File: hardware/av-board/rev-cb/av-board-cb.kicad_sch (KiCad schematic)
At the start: 291 parts, among them J1 RCA Y, J11 XIAO 5V..D7, J12 XIAO D0..D6, J13 OPTICAL, J14 RCA S/PDIF, J15 USB-C 5V, J16 JTAG, J2 RCA Pb, J20 DF40HC(3.0)-80DS, J21 DF40HC(3.0)-100DS, J22 DF40HC(3.0)-100DS, J3 RCA Pr, J4 RCA L, J5 RCA R, J6 HDMI-001, J7 SYNC, J8 VGA, Q1 2N7002, Q2 2N7002, Q3 2N7002, Q4 2N7002, Q5 2N7002, SW1 TS-1187A-B-A-B, SW2 TS-1187A-B-A-B, SW3 TS-1187A-B-A-B, U1 ADV7181DBCPZ-RL, U10 TPD4E05U06DQAR, U12 TPS7A2045PDBVR, U13 SN74LVC1GU04DBVR, U14 SN74LVC1G04DBVR, U15 SN74LVC1G04DBVR, U17 MS5351M, U18 ME6211C25M5G-N, U19 TPD4E05U06DQAR, U2 SN65DP159RGZR, U20 TPD4E05U06DQAR, U21 SN74LVC2G17DBVR, U22 SN74LVC8T245PWR, U23 SN74AVC4T245PWR, U24 ME6211C30M5G-N, U3 PCM1808PWR, U4 TLV62569DBVR, U5 TPS7A7001DDAR, U6 TPS7A7001DDAR, U7 TLV62569DBVR, U8 TPD4E05U06DQAR, U9 TPD4E05U06DQAR, Y1 28.63636MHz 20pF, Y2 25MHz 10pF

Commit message: AV boards: the last complete, valid design of each revision; decoupling at the pins
Each revision's board, schematic, fab files and renders are its last complete
route: DRC clean, no unconnected items, ERC clean, the board equal to its
schematic part for part (pads, values, footprints; only the mounting holes
H1-H4 have no symbol).

- Rev A: the silkscreen pass (labels clear of pads, texts and part bodies);
  copper unchanged.
- Rev B: the previous route with the silkscreen pass. Its schematic stays the
  one it was routed from: board.py now numbers eight capacitors the other way
  round, and its placement fixes (below) are not routed yet, the routes on the
  new placement having left 1 and 3 connections (review.md, Status).
- C-A: routed again on the fixed placement (try-ca-p1), the copper the router
  laid twice over taken up (218 segments).
- C-B: S/PDIF on rev B's 5-pin header instead of the coax jack, the HDMI
  receptacle next to the RCAs, the board 100 x 100 mm; routed again on the
  fixed placement (try-cb-p3). 5.4 mm of copper laid side by side in five
  nets is left (rev-c/review.md).

The review found decoupling not at the pins on every board (ADV7511 9-25 mm,
DP159 6-13 mm, the bucks' input capacitor by EN, the LDOs' capacitors, the
clock LDOs 73-80 mm from their chip) and C's VBUS_IN 0.25 mm wide for 2 A:
- parts.py: Part.at = "REF.PAD", the one pad a capacitor or filter serves;
  circuits, carrier.py and board.py name it for every regulator and supply pin
- pcbkit.py placer: ESD parts first, then small chips, then the at= capacitors
  and bias parts in board.py order; mean pin-to-capacitor distance on the
  placements: rev B 8.1 -> 3.6 mm, C-A 6.3 -> 3.3, C-B 5.5 -> 3.4
- rev C: VBUS_IN 0.7/1.2 mm into the TVS and fuse; rev B and C: the coax
  slicer placed first (SPDIF_AC a bias net); rev B: the buck U4 turned over

Kit: the silkscreen pass (labels clear of pads, texts, parts and the SOM,
reserved in the placer); prune takes up copper lying on another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
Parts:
- removed J14: RCA S/PDIF, lcsc:CONN-TH_RCJ-011, symbol lcsc:RCJ-017
- C11, C8: value 10u -> 220p; footprint Capacitor_SMD:C_0805_2012Metric -> Capacitor_SMD:C_0402_1005Metric; LCSC C15850 -> C1530
- C12, C9: value 220p -> 10u; footprint Capacitor_SMD:C_0402_1005Metric -> Capacitor_SMD:C_0805_2012Metric; LCSC C1530 -> C15850
- C5, C85: value 10u -> 6.8p; footprint Capacitor_SMD:C_0805_2012Metric -> Capacitor_SMD:C_0402_1005Metric; LCSC C15850 -> C1576
- C6, C86: value 6.8p -> 10u; footprint Capacitor_SMD:C_0402_1005Metric -> Capacitor_SMD:C_0805_2012Metric; LCSC C1576 -> C15850
- J13: value OPTICAL -> SPDIF; footprint lcsc:HDR-TH_3P-P2.54-V-M_PZ254V-11-03P -> lcsc:HDR-TH_5P-P2.54-V-M; symbol lcsc:PZ254V-11-03P_C2937625 -> lcsc:PZ254V-11-05P; LCSC C2937625 -> C492404
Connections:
- net FB_1V1: now also C85.2; no longer C86.2
- net FB_1V8A: now also C11.2; no longer C12.2
- net FB_3V3: now also C8.2; no longer C9.2
- net FB_3V6: now also C5.2; no longer C6.2
- net GND: now also C12.2, C6.2, C86.2, C9.2, J13.4; no longer C11.2, C5.2, C8.2, C85.2
- net IN_KEY1: now also J20.75; no longer J21.5
- net IN_KEY2: now also J20.73; no longer J21.7
- net IN_LED: now also J20.71; no longer J21.11
- net SPDIF_5V: now also J13.5; no longer J13.3
- net SPDIF_COAX: now also J13.1
- net SPDIF_OPT: now also J13.3; no longer J13.1
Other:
- moved on the sheet: C11, C12, C5, C6, C65, C66, C67, C68, C69, C8, C80, C81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

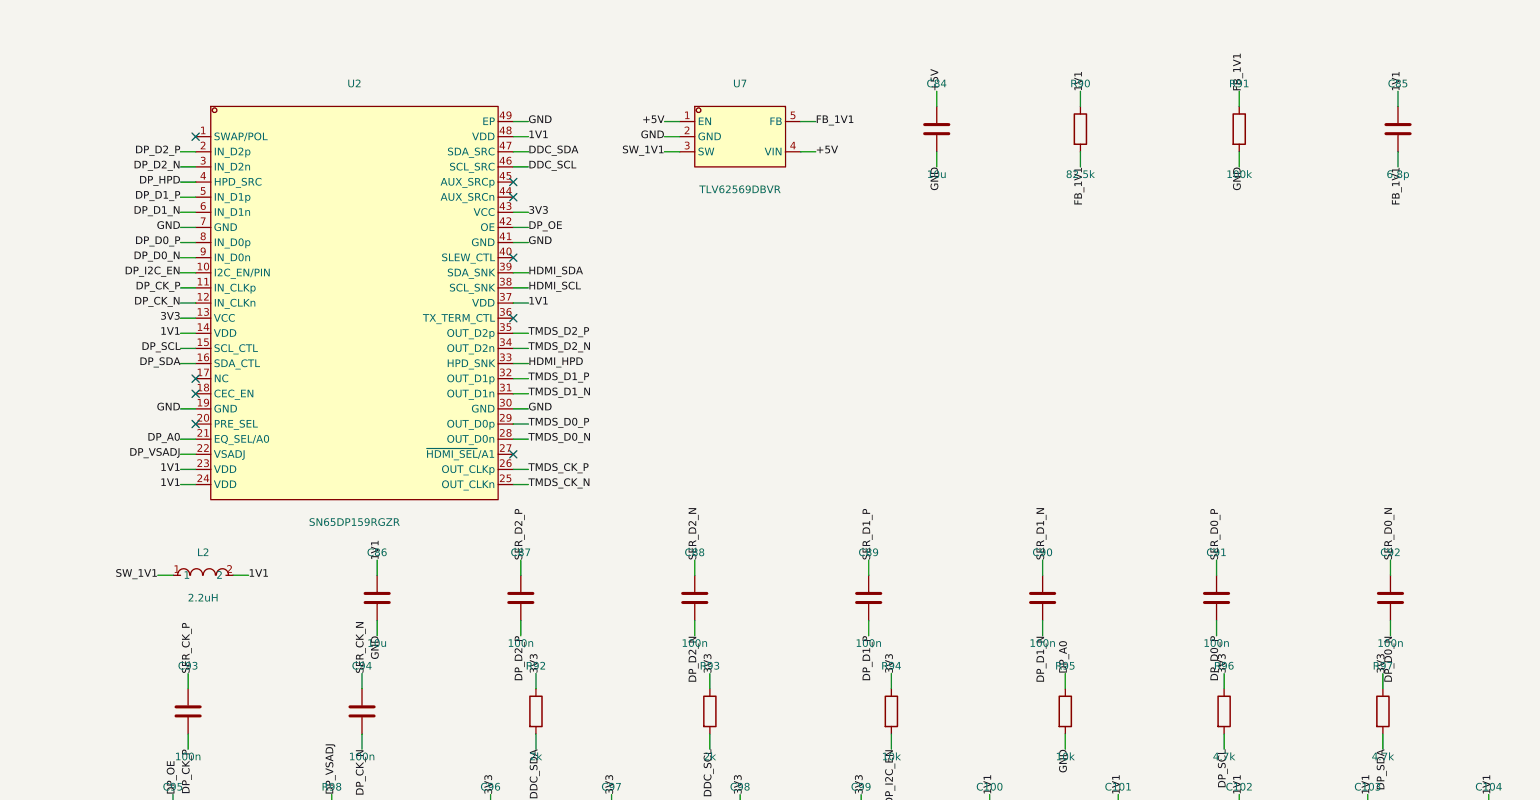
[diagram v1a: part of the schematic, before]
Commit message: AV boards: rev B, C-B routed on the fixed placement; prune side-by-side copies; JLC jack rotation
Every revision: schematic = board.py, the board = its schematic part for part,
ERC and DRC clean, no unconnected items; rev B's, C-A's and C-B's review tables
measured on these routes.

- Rev B: routed on the capacitor placement fixes (try-b-r1, its last gap
  finished); schematic regenerated (eight capacitors renumbered).
- C-B: the 1V1 buck's inductor and output capacitor placed before its feedback
  divider: in the 3V6 bucks' order the divider's 6.8 pF took the inductor's place
  beside SW, the inductor went above the chip with its SW pad turned away (10.7 mm
  of SW track, FB's copper 0.2 mm from it). Routed again (try-cb-q3): SW 4.1 mm,
  FB 3.0 mm from it; nothing digital within 0.5 mm of an analog line but XTAL1
  beside LLC at the pins' pitch.
- C-A: its review column measured on the route; CPL jack rotations.
- kit/pcbkit.py prune: copper laid side by side taken up too (beside(): the
  shorter of each kit/doubled.py pair), every candidate checked by DRC on a copy
  of the file's text first (save_without(), removable()), so nothing taken out of
  a pcbnew board is put back; rounds run with faulthandler and report a crash's
  signal (one round had segfaulted in libstdc++ with no message).
- kit/pcbkit.py finish_unconnected: a gap's three nearest pad pairs tried in turn
  (rev B's TX_PLVDD pin 21 was walled in towards pin 26, not towards its own
  capacitor).
- kit/gen_fab.py JLC_TURN: JLCPCB places a part by its own footprint for the LCSC
  number; for RCJ-014 and RCJ-017 that is ours turned 90 degrees, so the CPL
  turns those jacks back (their preview had the barrels along the board edge).
  RCJ-012 has no footprint there and is placed as drawn.

Co-Authored-By: Claude Opus 5.5 <noreply@anthropic.com>
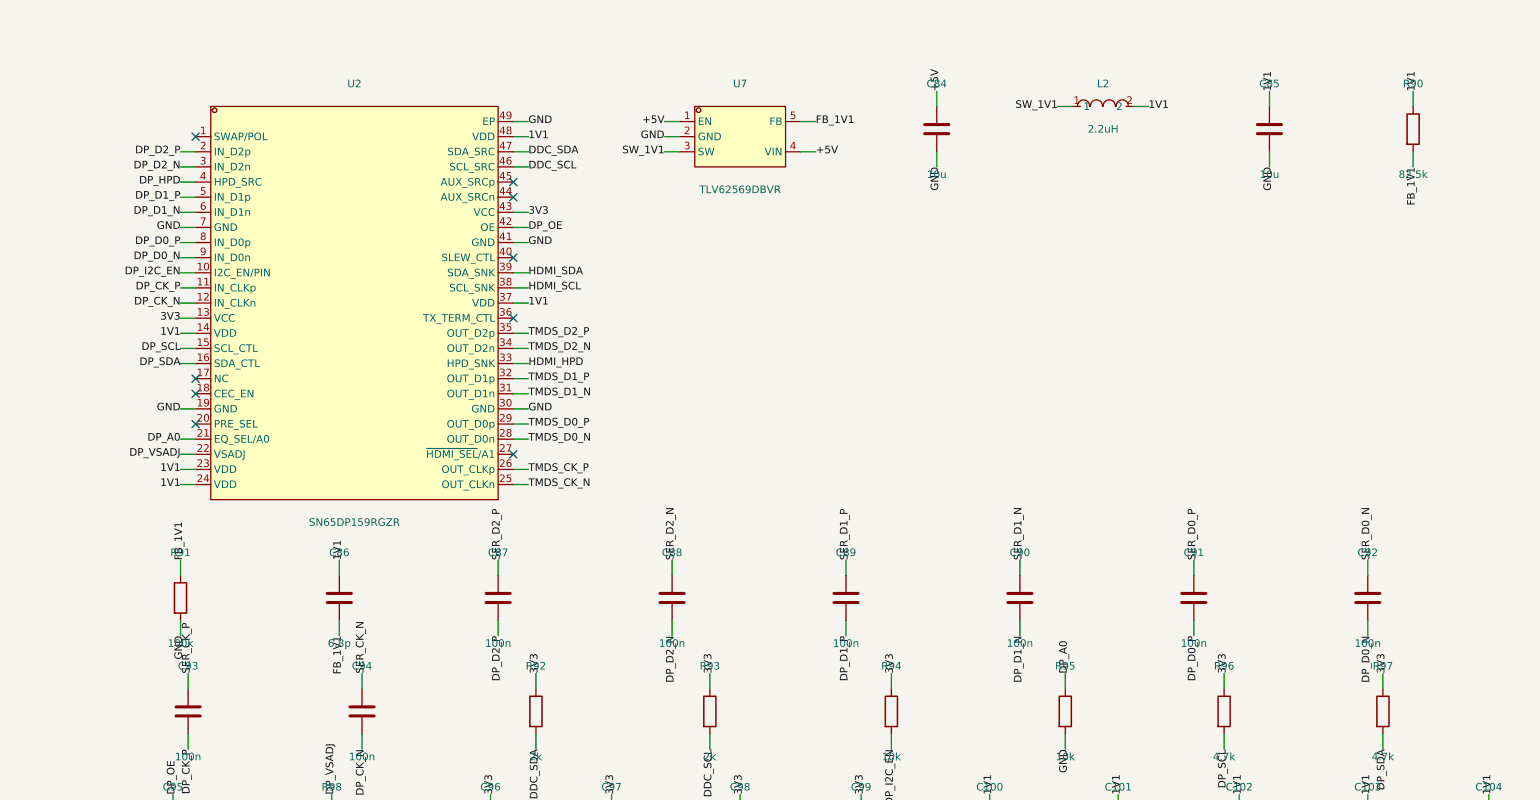
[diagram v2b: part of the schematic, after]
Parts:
- C85: value 6.8p -> 10u; footprint Capacitor_SMD:C_0402_1005Metric -> Capacitor_SMD:C_0805_2012Metric; LCSC C1576 -> C15850
- C86: value 10u -> 6.8p; footprint Capacitor_SMD:C_0805_2012Metric -> Capacitor_SMD:C_0402_1005Metric; LCSC C15850 -> C1576
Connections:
- net FB_1V1: now also C86.2; no longer C85.2
- net GND: now also C85.2; no longer C86.2
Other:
- moved on the sheet: C85, C86, C87, C88, C89, C90, C91, C92, L2, R90, R91

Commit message: AV board C-B: a protected debug header and test pads; the kit on KiCad 10, a second host
C-B (the SOM hides the FPGA's pins, so the board brings out what bring-up needs):
- J17, a 2 x 8 header left of the SOM: the ADV7181D's, the DP159's and the MS5351M's I2C, six
  spare FPGA pins, J22's nearest (dbg0-dbg5: AB16 L13 M13 AA16 AB17 Y17, LVCMOS33 in
  fpga/av-board-cb.cst), a 3.3 V reference and ground, labelled pin by pin, "DEBUG" above it.
  Every pin but ground through 220 R by the header (C25091, as Digilent's Pmod ports): a slipped
  probe or a wrong wire drives at most 15 mA into a pin; VREF, beside ground, is a reference
  (50 mW in its resistor when shorted), not a supply.
- A bare test pad on each rail by its regulator (+5V 3V6 3V3 1V8 1V1 3V0 2V5 5VA), labelled,
  and two ground pads with holes for a wire loop. Not assembled.
- The DP159's ground pins 19 and 41 now reach into its exposed pad: their fanout stubs stopped
  0.22 mm short of it, the prune pass took them up, and pin 19 was left open
  (gen_pcb.py serdes()).
- Re-routed: the best of a batch (v5): DRC 0 errors, 0 unconnected; schematic = board.py =
  board (1064 pins); fab files, renders and rev-c/review.md's layout numbers updated. Three
  resistors after the debug block are renumbered (R100-R102 -> R113-R115).
- Known, fixes next: an HDMI 2.0 layout audit against TI's SN65DP159 and SPRAAR7 guidelines
  finds other nets' vias against the TMDS run (their plane antipads within 0.01-0.21 mm),
  pairs 3W apart (TI: 5W), the transceivers' reference clock autorouted as two single lines,
  a crystal and a mounting hole near the lines, and no plane voids under the pads on them.

rev-c/review.md: kit/xtalk.py measures analog tracks against digital tracks only; KiCad's DRC
with the 0.5 mm rule as a custom rule counts vias too, and finds two of RCA_SYNC's vias 0.27 mm
from the VGA DDC clock on C-A (the C-A text said nothing but XTAL1/LLC came that close).

Kit:
- main(): the board made with its project (pcbn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
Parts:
- added J17: DEBUG, lcsc:HDR-TH_16P-P2.54-V-M-R2-C8-S2.54, symbol lcsc:Header-Male-2.54_2x8
- added R103, R104, R105, R106, R107, R108, R109, R110, R111, R112: 220, Resistor_SMD:R_0402_1005Metric, symbol Device:R
- added R113: 1k, Resistor_SMD:R_0402_1005Metric, symbol Device:R
- added R114, R115: 5.1k, Resistor_SMD:R_0402_1005Metric, symbol Device:R
- added TP1: +5V, TestPoint:TestPoint_Pad_D1.5mm, symbol Connector:TestPoint
- added TP10, TP9: GND, TestPoint:TestPoint_THTPad_D2.0mm_Drill1.0mm, symbol Connector:TestPoint
- added TP2: 3V6, TestPoint:TestPoint_Pad_D1.5mm, symbol Connector:TestPoint
- added TP3: 3V3, TestPoint:TestPoint_Pad_D1.5mm, symbol Connector:TestPoint
- added TP4: 1V8A, TestPoint:TestPoint_Pad_D1.5mm, symbol Connector:TestPoint
- added TP5: 1V1, TestPoint:TestPoint_Pad_D1.5mm, symbol Connector:TestPoint
- added TP6: 3V0, TestPoint:TestPoint_Pad_D1.5mm, symbol Connector:TestPoint
- added TP7: 2V5, TestPoint:TestPoint_Pad_D1.5mm, symbol Connector:TestPoint
- added TP8: 5VA, TestPoint:TestPoint_Pad_D1.5mm, symbol Connector:TestPoint
- R100: value 1k -> 220; LCSC C11702 -> C25091; Note (none) -> debug header pin protection
- R101, R102: value 5.1k -> 220; LCSC C25905 -> C25091; Note (none) -> debug header pin protection
- SO1, SO2, SO3, SO4: now left out of the parts list
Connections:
- net +5V: now also TP1.1
- net 1V1: now also TP5.1
- net 1V8A: now also TP4.1
- net 2V5: now also TP7.1
- net 3V0: now also TP6.1
- net 3V3: now also R113.1, TP3.1
- net 3V6: now also TP2.1
- net 5VA: now also TP8.1
- net DP_SCL: now also R103.1
- net DP_SDA: now also R104.1
- net GND: now also J17.15, J17.16, J17.2, R114.2, R115.2, TP10.1, TP9.1; no longer R101.2, R102.2
- net IN_SCL: now also R101.1
- net IN_SDA: now also R102.1
- net MODE0: now also R113.2; no longer R100.2
- net MODE1: now also R114.1; no longer R101.1
- net MODE2: now also R115.1; no longer R102.1
- net PLL_SCL: now also R105.1
- net PLL_SDA: now also R106.1
- net DBG5: now reaches J22.26
- net DBG5: now also R112.1
- net DBG4: now reaches J22.28
- net DBG4: now also R111.1
- net DBG3: now reaches J22.30
- net DBG3: now also R110.1
- net DBG2: now reaches J22.32
- net DBG2: now also R109.1
- net DBG1: now reaches J22.34
- net DBG1: now also R108.1
- net DBG0: now reaches J22.36
- net DBG0: now also R107.1
- new net DBG0_J: J17.9, R107.2
- new net DBG1_J: J17.10, R108.2
- new net DBG2_J: J17.11, R109.2
- new net DBG3_J: J17.12, R110.2
- new net DBG4_J: J17.13, R111.2
- new net DBG5_J: J17.14, R112.2
- new net DBG_VREF: J17.1, R100.2
- new net DP_SCL_J: J17.5, R103.2
- new net DP_SDA_J: J17.6, R104.2
- new net IN_SCL_J: J17.3, R101.2
- new net IN_SDA_J: J17.4, R102.2
- new net PLL_SCL_J: J17.7, R105.2
- new net PLL_SDA_J: J17.8, R106.2
- no-connect marks 189 -> 183
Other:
- moved on the sheet: C108, C109, C110, C111, J20, J21, J22, R100, R101, R102, SO1, SO2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
